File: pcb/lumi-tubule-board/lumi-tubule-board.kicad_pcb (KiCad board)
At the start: 2 copper layers, 83.1 x 83 mm, 74 parts, among them Q1 DMN1045UFR4, Q10 DMN1045UFR4, Q11 DMN1045UFR4, Q12 DMN1045UFR4, Q13 DMN1045UFR4, Q2 DMN1045UFR4, Q3 DMN1045UFR4, Q4 DMN1045UFR4, Q5 DMN1045UFR4, Q6 DMN1045UFR4, Q7 DMN1045UFR4, Q8 DMN1045UFR4, Q9 DMN1045UFR4, SW1 SWITCH_TACT_SMT4.6X2.8, SW2 SWITCH_TACT_SMT4.6X2.8, U1 SHTC3, U2 VREG_SOT23-5, U3 ESP32-S3-MINI-1, U4 LIS2Dx12, X1 USB_C

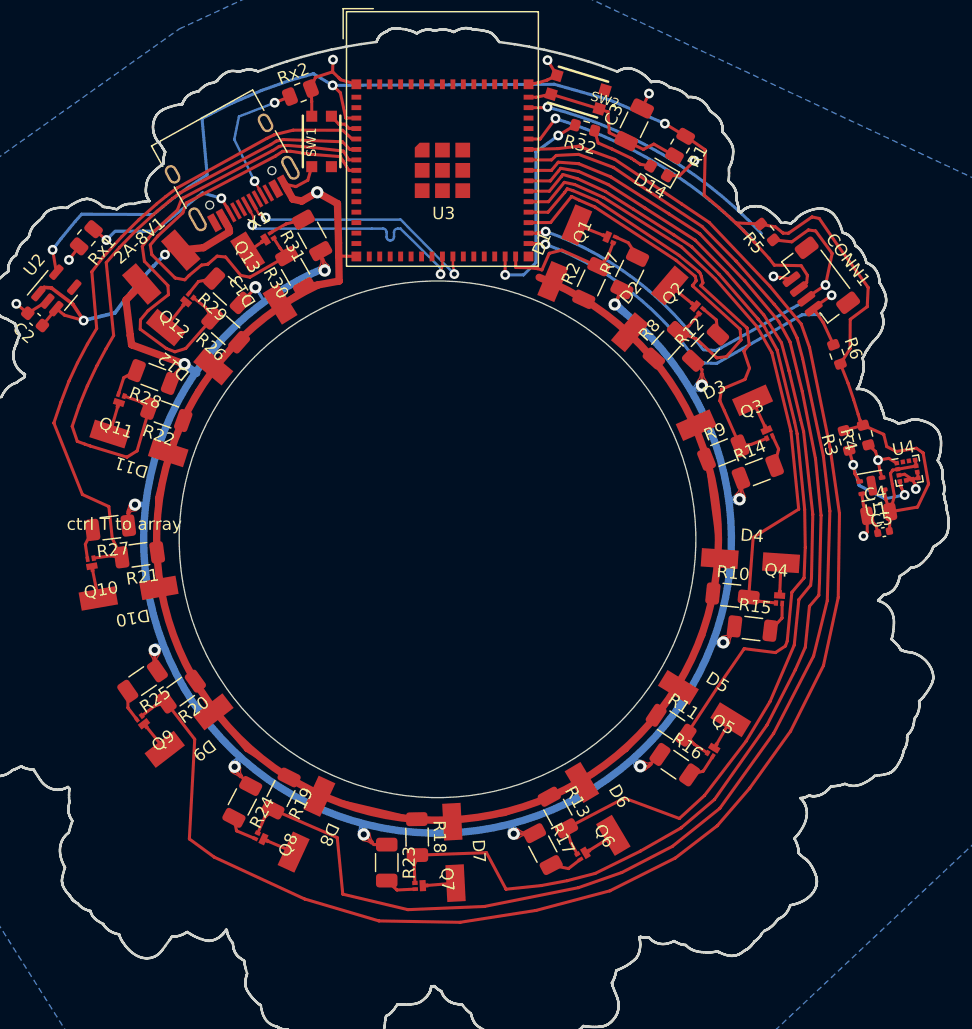
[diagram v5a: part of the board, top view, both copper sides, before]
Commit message: Correct and complete traces
Redid ugly traces and connected SDA/SCL lines to new ground plane design.
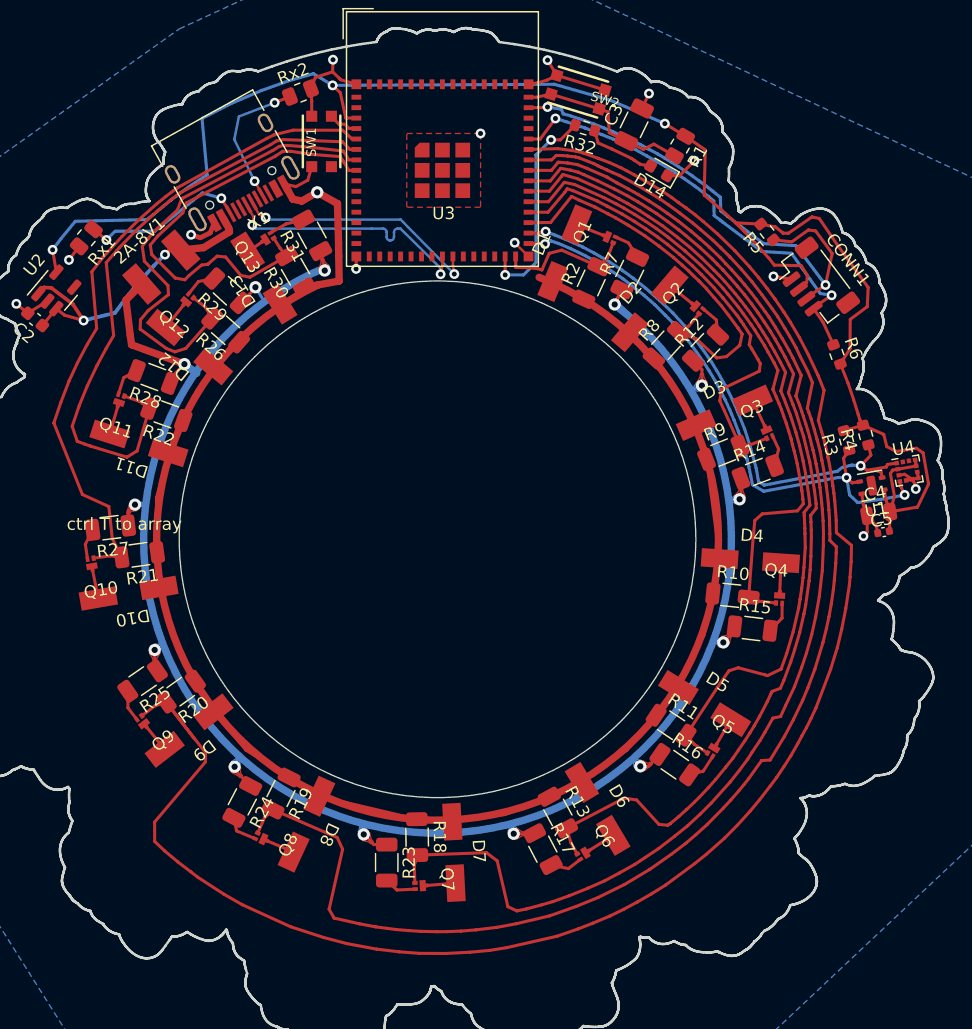
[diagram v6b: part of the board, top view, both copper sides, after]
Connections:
- U3 pad 61: Net-(U3-Pad61) -> GND
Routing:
- net SCL_int: track 6.03 -> 44.8 mm
- net SDA: track 11.8 -> 40.0 mm
- net SCL: track 7.90 -> 35.9 mm
- net SDA_int: track 31.1 -> 47.7 mm
- net L9: track 132.0 -> 144.0 mm
- net GND: track 173.4 -> 181.2 mm, vias 10 -> 14
- net L8: track 114.1 -> 118.7 mm
- net L7: track 97.3 -> 99.8 mm
- net L4: track 50.4 -> 51.7 mm
- net L6: track 81.2 -> 82.2 mm
- net L5: track 65.5 -> 66.3 mm
- added copper zone on F.Cu, net GND

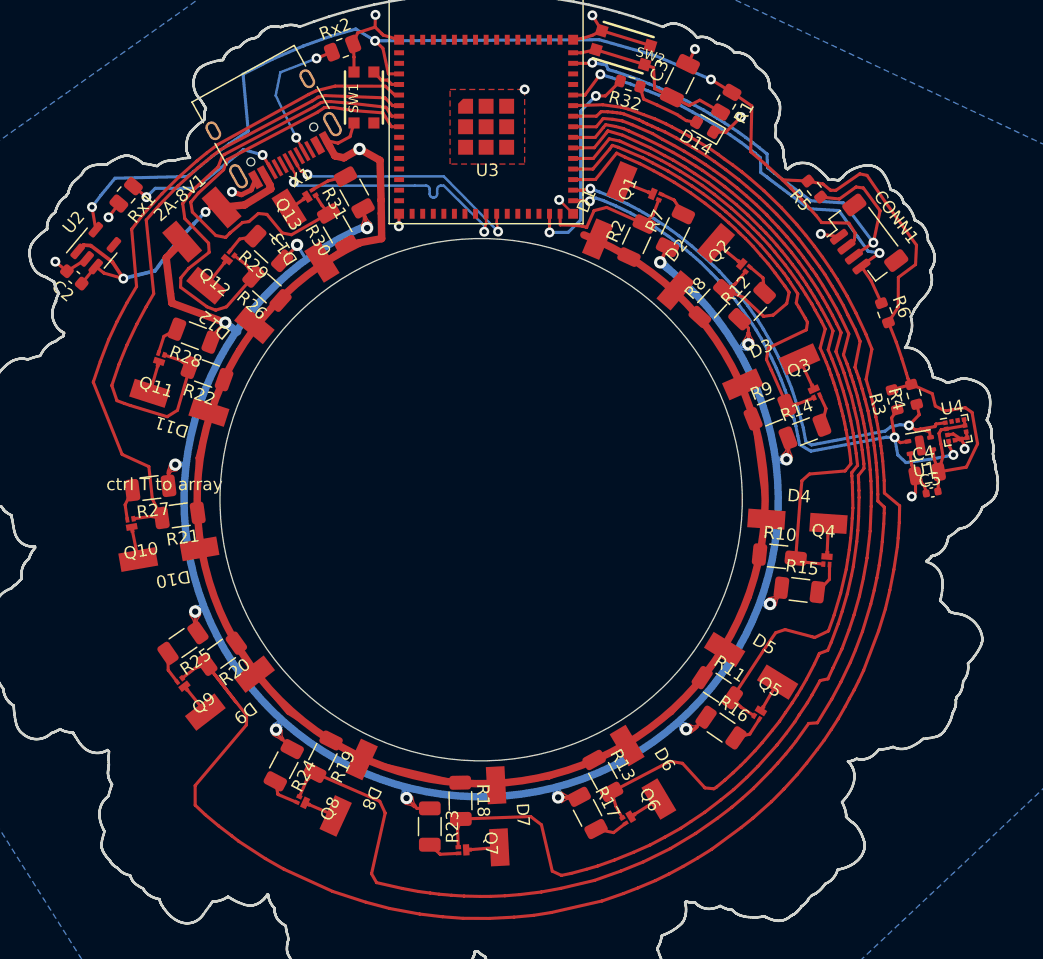
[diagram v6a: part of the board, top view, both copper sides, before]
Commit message: Fix MOSFET wiring
Fixed the MOSFETs' wiring, which was all wrong. Rerouted mosfet out via ground plane, freeing up space for the Vsup line on top of board. Removed the diagnosis LED line on the back of PCB which was interrupting ground plane flow. Swapped out the pulldown resistor for something smaller.
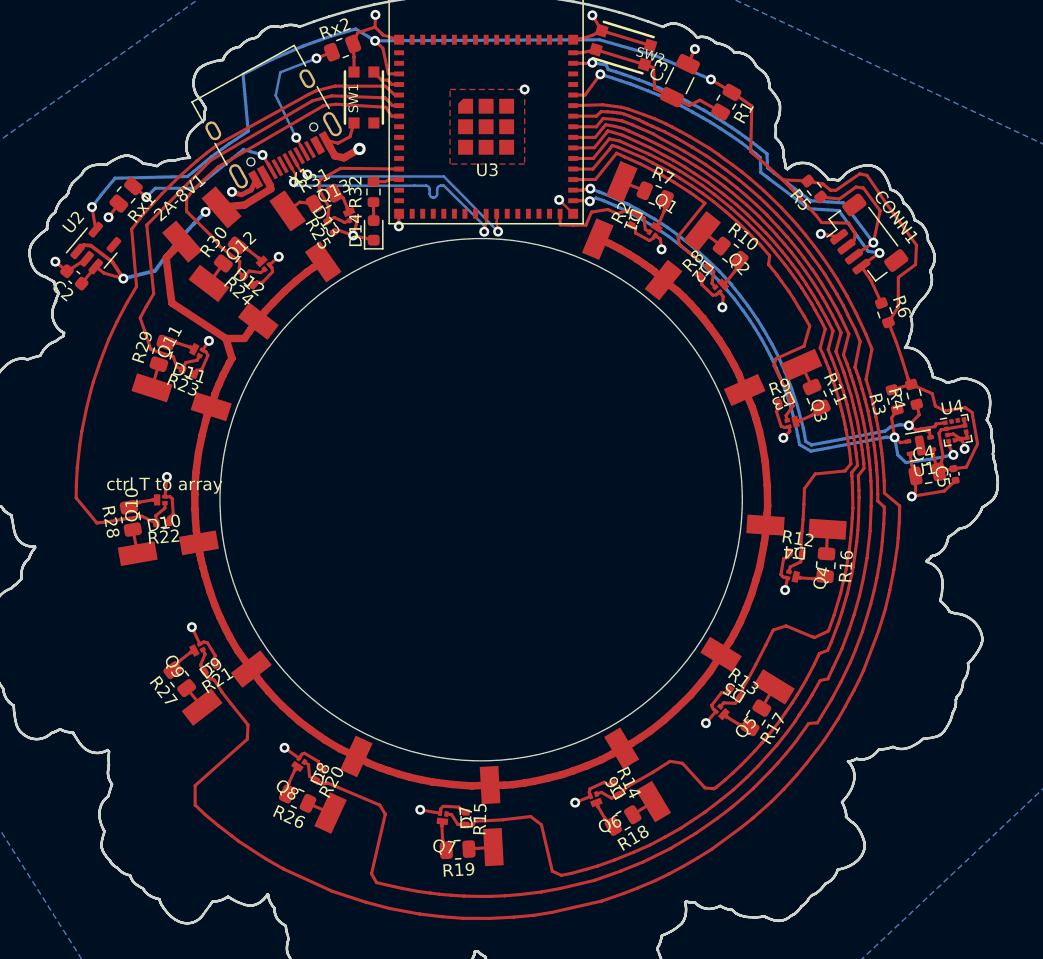
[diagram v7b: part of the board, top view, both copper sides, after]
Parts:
- R10, R11, R18, R19, R26, R30: value 10k -> 27; footprint Resistor_SMD:R_1206_3216Metric -> Resistor_SMD:R_0805_2012Metric
- R12, R14, R15, R23, R24, R25: value 18 -> 10k; footprint Resistor_SMD:R_1206_3216Metric -> Resistor_SMD:R_0402_1005Metric
- R13, R2, R20, R21, R22, R8, R9: footprint Resistor_SMD:R_1206_3216Metric -> Resistor_SMD:R_0402_1005Metric
- R16, R17, R27, R28, R29, R31, R7: value 18 -> 27; footprint Resistor_SMD:R_1206_3216Metric -> Resistor_SMD:R_0805_2012Metric
- moved R23 41.4 mm to (126.5, 89.7), turned to 157.3 degrees
- moved R26 41.1 mm to (135.2, 124.0), turned to 155.4 degrees
- moved R24 39.1 mm to (131.3, 82.4), turned to 137.6 degrees
- moved R25 35.5 mm to (137.9, 78.0), turned to 119.9 degrees
- moved R15 32.5 mm to (148.8, 125.7), turned to -91.9 degrees
- moved R14 32.5 mm to (160.8, 123.3), turned to -64.2 degrees
- moved D14 27.9 mm to (141.4, 78.3), turned to 90 degrees
- moved R10 24.7 mm to (170.1, 80.2), turned to -38.4 degrees
- moved R11 24.7 mm to (177.0, 91.8), turned to -66.1 degrees
- moved R32 22.4 mm to (141.3, 75.2), turned to 90 degrees
- moved R12 20.2 mm to (175.3, 104.3), turned to -8.8 degrees
- moved R16 15.5 mm to (177.7, 105.3), turned to -93.8 degrees
- moved R27 15.5 mm to (125.8, 114.4), turned to 127.7 degrees
- moved R17 15.5 mm to (172.1, 117.5), turned to -121.5 degrees
- moved R28 15.5 mm to (121.8, 101.5), turned to 100 degrees
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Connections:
- D1 pad 1: GND -> Net-(D1-Pad1)
- D1 pad 2: Net-(D1-Pad2) -> 5V-fused
- D10 pad 1: GND -> Net-(D10-Pad1)
- D10 pad 2: Net-(D10-Pad2) -> 5V-fused
- D11 pad 1: GND -> Net-(D11-Pad1)
- D11 pad 2: Net-(D11-Pad2) -> 5V-fused
- D12 pad 1: GND -> Net-(D12-Pad1)
- D12 pad 2: Net-(D12-Pad2) -> 5V-fused
- D13 pad 1: GND -> Net-(D13-Pad1)
- D13 pad 2: Net-(D13-Pad2) -> 5V-fused
- D2 pad 1: GND -> Net-(D2-Pad1)
- D2 pad 2: Net-(D2-Pad2) -> 5V-fused
- D3 pad 1: GND -> Net-(D3-Pad1)
- D3 pad 2: Net-(D3-Pad2) -> 5V-fused
- D4 pad 1: GND -> Net-(D4-Pad1)
- D4 pad 2: Net-(D4-Pad2) -> 5V-fused
- D5 pad 1: GND -> Net-(D5-Pad1)
- D5 pad 2: Net-(D5-Pad2) -> 5V-fused
- D6 pad 1: GND -> Net-(D6-Pad1)
- D6 pad 2: Net-(D6-Pad2) -> 5V-fused
- D7 pad 1: GND -> Net-(D7-Pad1)
- D7 pad 2: Net-(D7-Pad2) -> 5V-fused
- D8 pad 1: GND -> Net-(D8-Pad1)
- D8 pad 2: Net-(D8-Pad2) -> 5V-fused
- D9 pad 1: GND -> Net-(D9-Pad1)
- D9 pad 2: Net-(D9-Pad2) -> 5V-fused
- Q1 pad 1: Net-(D1-Pad2) -> Net-(Q1-Pad1)
- Q1 pad 3: Net-(Q1-Pad3) -> GND
- Q10 pad 1: Net-(D10-Pad2) -> Net-(Q10-Pad1)
- Q10 pad 3: Net-(Q10-Pad3) -> GND
- Q11 pad 1: Net-(D11-Pad2) -> Net-(Q11-Pad1)
- Q11 pad 3: Net-(Q11-Pad3) -> GND
- Q12 pad 1: Net-(D12-Pad2) -> Net-(Q12-Pad1)
- Q12 pad 3: Net-(Q12-Pad3) -> GND
- Q13 pad 1: Net-(D13-Pad2) -> Net-(Q13-Pad1)
- Q13 pad 3: Net-(Q13-Pad3) -> GND
- Q2 pad 1: Net-(D2-Pad2) -> Net-(Q2-Pad1)
- Q2 pad 3: Net-(Q2-Pad3) -> GND
- Q3 pad 1: Net-(D3-Pad2) -> Net-(Q3-Pad1)
- Q3 pad 3: Net-(Q3-Pad3) -> GND
- Q4 pad 1: Net-(D4-Pad2) -> Net-(Q4-Pad1)
- Q4 pad 3: Net-(Q4-Pad3) -> GND
- Q5 pad 1: Net-(D5-Pad2) -> Net-(Q5-Pad1)
- Q5 pad 3: Net-(Q5-Pad3) -> GND
- Q6 pad 1: Net-(D6-Pad2) -> Net-(Q6-Pad1)
- Q6 pad 3: Net-(Q6-Pad3) -> GND
- Q7 pad 1: Net-(D7-Pad2) -> Net-(Q7-Pad1)
- Q7 pad 3: Net-(Q7-Pad3) -> GND
- Q8 pad 1: Net-(D8-Pad2) -> Net-(Q8-Pad1)
- Q8 pad 3: Net-(Q8-Pad3) -> GND
- Q9 pad 1: Net-(D9-Pad2) -> Net-(Q9-Pad1)
- Q9 pad 3: Net-(Q9-Pad3) -> GND
- R10 pad 1: GND -> Net-(D2-Pad1)
- R10 pad 2: L4 -> Net-(Q2-Pad1)
- R11 pad 1: GND -> Net-(D3-Pad1)
- R11 pad 2: L5 -> Net-(Q3-Pad1)
- R12 pad 1: 5V-fused -> GND
- R12 pad 2: Net-(Q2-Pad3) -> L4
- R13 pad 2: L6 -> L5
- R14 pad 1: 5V-fused -> GND
- R14 pad 2: Net-(Q3-Pad3) -> L6
- R15 pad 1: 5V-fused -> GND
- R15 pad 2: Net-(Q4-Pad3) -> L7
- R16 pad 1: 5V-fused -> Net-(D4-Pad1)
- R16 pad 2: Net-(Q5-Pad3) -> Net-(Q4-Pad1)
- R17 pad 1: 5V-fused -> Net-(D5-Pad1)
- R17 pad 2: Net-(Q6-Pad3) -> Net-(Q5-Pad1)
- R18 pad 1: GND -> Net-(D6-Pad1)
- R18 pad 2: L7 -> Net-(Q6-Pad1)
- R19 pad 1: GND -> Net-(D7-Pad1)
- R19 pad 2: L8 -> Net-(Q7-Pad1)
- R20 pad 2: L9 -> L8
- R21 pad 2: L10 -> L9
- R22 pad 2: L11 -> L10
- R23 pad 1: 5V-fused -> GND
- R23 pad 2: Net-(Q7-Pad3) -> L11
- R24 pad 1: 5V-fused -> GND
- R24 pad 2: Net-(Q8-Pad3) -> L12
- R25 pad 1: 5V-fused -> GND
- R25 pad 2: Net-(Q9-Pad3) -> L13
- R26 pad 1: GND -> Net-(D8-Pad1)
- R26 pad 2: L12 -> Net-(Q8-Pad1)
- R27 pad 1: 5V-fused -> Net-(D9-Pad1)
- R27 pad 2: Net-(Q10-Pad3) -> Net-(Q9-Pad1)
- R28 pad 1: 5V-fused -> Net-(D10-Pad1)
- R28 pad 2: Net-(Q11-Pad3) -> Net-(Q10-Pad1)
- R29 pad 1: 5V-fused -> Net-(D11-Pad1)
- R29 pad 2: Net-(Q12-Pad3) -> Net-(Q11-Pad1)
- R30 pad 1: GND -> Net-(D12-Pad1)
- R30 pad 2: L13 -> Net-(Q12-Pad1)
- R31 pad 1: 5V-fused -> Net-(D13-Pad1)
- R31 pad 2: Net-(Q13-Pad3) -> Net-(Q13-Pad1)
- R7 pad 1: 5V-fused -> Net-(D1-Pad1)
- R7 pad 2: Net-(Q1-Pad3) -> Net-(Q1-Pad1)
- U3 pad 12: unconnected-(U3-Pad12) -> L13
- U3 pad 13: unconnected-(U3-Pad13) -> LED
- U3 pad 15: unconnected-(U3-Pad15) -> (no net)
- U3 pad 29: LED -> (no net)
- U3 pad 61: GND -> Net-(U3-Pad61)
- U3 pad 8: L13 -> (no net)
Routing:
- net GND: track 181.2 -> 99.2 mm, vias 14 -> 26
- net 5V-fused: track 171.6 -> 133.6 mm, vias 13 -> 0
- net L13: track 36.4 -> 12.1 mm
- net LED: track 17.4 -> 2.10 mm, vias 2 -> 0
- net L2: track 31.9 -> 20.7 mm
- net L11: track 50.5 -> 39.8 mm
- net L12: track 39.2 -> 30.2 mm
- net Net-(D14-Pad2): track 5.73 -> 1.48 mm
- net L9: track 144.0 -> 139.9 mm
- net L10: track 54.1 -> 57.9 mm
- net Net-(Q13-Pad3): track 2.91 -> 0.00 mm
- net Net-(Q8-Pad3): track 2.72 -> 0.00 mm
- net Net-(D2-Pad2): track 2.67 -> 0.00 mm
- net Net-(D1-Pad2): track 2.67 -> 0.00 mm
- net Net-(D3-Pad2): track 2.67 -> 0.00 mm
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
